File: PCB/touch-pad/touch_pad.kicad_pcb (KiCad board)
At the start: 2 copper layers, 60.6 x 50.7 mm, 13 parts

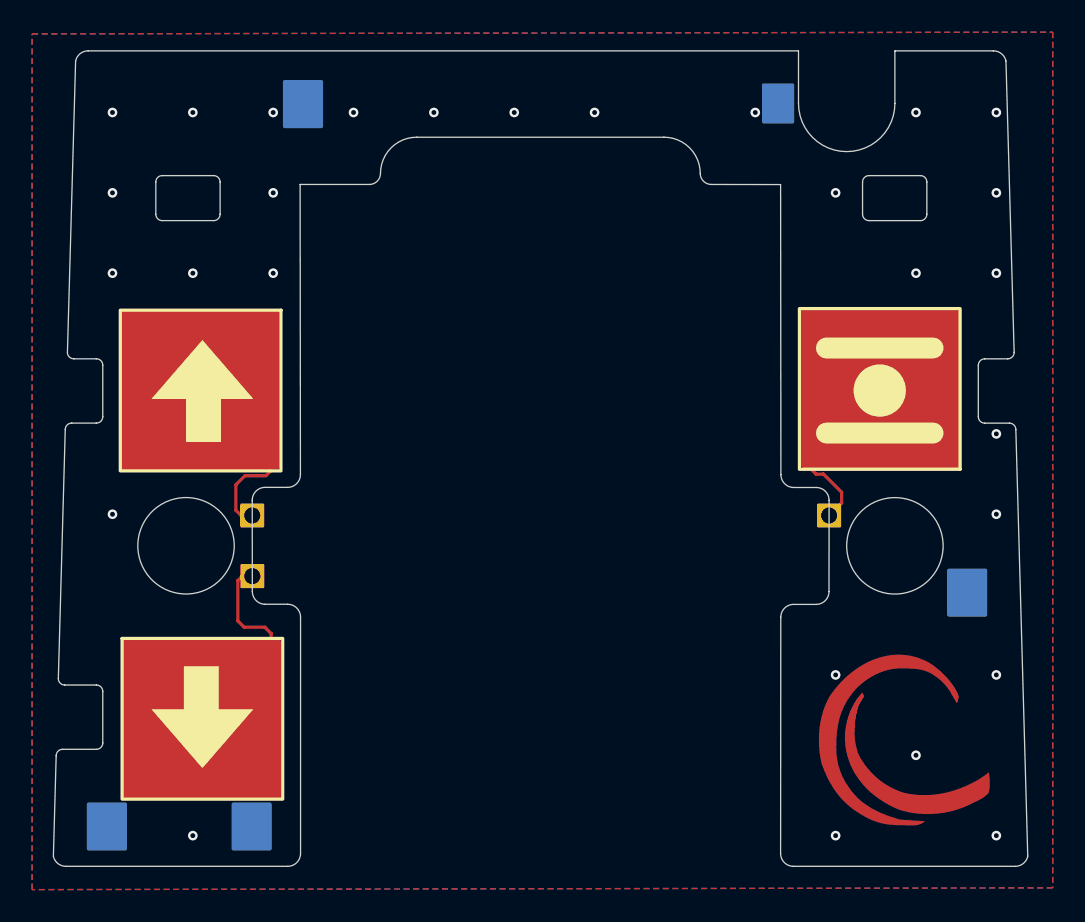
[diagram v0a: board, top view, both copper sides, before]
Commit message: Import v2.0 development state from Bitbucket branch v2.0
Overlay of the v2.0 design work onto the restructured PCB/ layout:
- airgradient-go-main v2.0 WIP: 186 footprints, microSD, PS1-CO,
  Birdy schematic review fixes; adds v2.0 BOM CSVs
- touch-pad v2.0: T1-T3 pads wired to touch controller CS channels,
  +3.1V rail renamed to VCC
- scd4x-module: minor updates
- libraries: new parts (SPL07-003, BM05B-SRSS-TB, PS1-CO, battery
  holder, ESP32-C5 models) and updated footprints; all library and
  3D model references normalized to ${KIPRJMOD}-relative paths
- led_pcb board was dropped in v2.0 (never migrated)

Known open items carried over from review: U14 VDD_IO not yet
connected to the 3.1V rail; U19 (LM66200) still fitted.
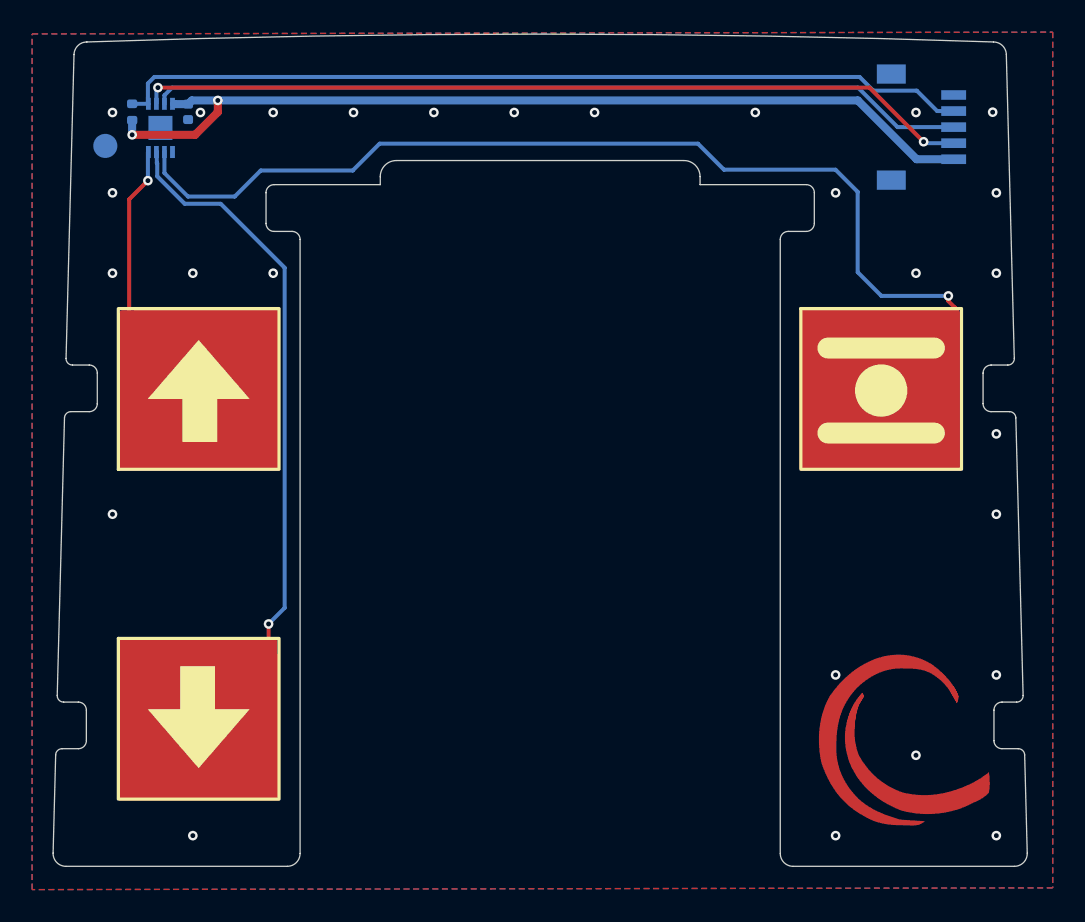
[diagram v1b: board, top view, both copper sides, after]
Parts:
- removed ? (x8): , 
- added C42: 0.1uF/25V, Capacitor_SMD:C_0402_1005Metric, B.Cu at (29.6, 25.2)
- added CN1: SM05B-SRSS-TB (LF)(SN), easyeda2kicad-oaf:CONN-SMD_SM05B-SRSS-TB-LF-SN, B.Cu at (75.3, 26.1)
- added R38: 100K, Resistor_SMD:R_0402_1005Metric, B.Cu at (26.1, 25.2)
- added TP1: TestPoint, TestPoint:TestPoint_Pad_D1.5mm, B.Cu at (24.4, 27.3)
- added U11: CAP1203-1-AC3-TR, easyeda2kicad-oaf:TDFN-8_L3.0-W2.0-P0.50-BL-EP, B.Cu at (27.9, 26.2)
- T1, T2, T3: footprint Library:tourch_pad -> Library-oaf:tourch_pad
- moved T1 0.34 mm to (30.1, 42.4), turned to 90 degrees
- moved T2 0.23 mm to (30.2, 62.8)
- moved T3 0.22 mm to (72.7, 42.3), turned to 0 degrees
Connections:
- T1 pad 1: unconnected-(T1-Pad1) -> Net-(U11-CS1)
- T2 pad 1: unconnected-(T2-Pad1) -> Net-(U11-CS2)
- T3 pad 1: unconnected-(T3-Pad1) -> Net-(U11-CS3)
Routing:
- net Net-(U11-CS3): track 0.00 -> 60.2 mm, vias 0 -> 1
- net VCC: track 0.00 -> 57.7 mm, vias 0 -> 2
- net /INT: track 0.00 -> 53.5 mm
- net /SDA: track 0.00 -> 52.0 mm, vias 0 -> 2
- net /SCL: track 0.00 -> 50.9 mm
- net Net-(U11-CS2): track 0.00 -> 36.0 mm, vias 0 -> 1
- net Net-(U11-CS1): track 0.00 -> 11.0 mm, vias 0 -> 1
- net unconnected-(T2-Pad1): track 6.96 -> 0.00 mm
- net unconnected-(T1-Pad1): track 5.98 -> 0.00 mm
- net unconnected-(T3-Pad1): track 4.94 -> 0.00 mm
- net GND: vias 28 -> 27
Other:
- board size 60.6 x 50.7 mm -> 60.6 x 51.8 mm
- board text added: "AG-TOUCH-GO-v2.0"
- board text removed: "${REFERENCE}"
- board text removed: "AG-TOUCH-GO-v1.0"

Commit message: Create production files; switch touch pad connector to Hong Cheng
Mainboard:
- Export v2.0 production files (gerbers, BOM, positions) and 3D STEP model
- Add BOM.csv export

Touch pad:
- Change CN1 connector manufacturer from JST to Hong Cheng HCZZ0032-5 (same housing)
- Regenerate production files as v2.0 (BOM now includes full parts list)
- Add Hong Cheng connector symbol, footprint, and 3D model to easyeda2kicad library
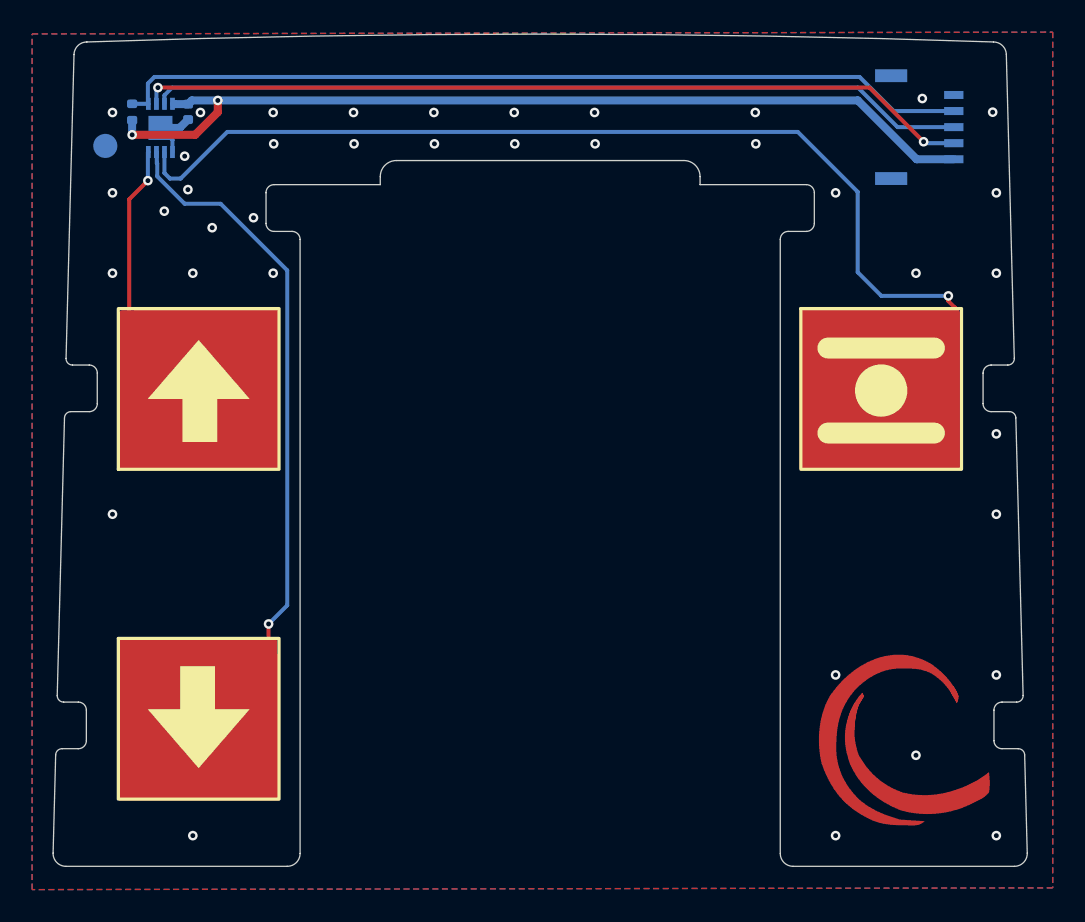
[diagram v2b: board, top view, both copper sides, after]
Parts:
- CN1: value SM05B-SRSS-TB (LF)(SN) -> HCZZ0032-5; footprint easyeda2kicad-oaf:CONN-SMD_SM05B-SRSS-TB-LF-SN -> easyeda2kicad-oaf:CONN-SMD_HCZZ0032-5
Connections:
- U11 pad 9: unconnected-(U11-EP-Pad9) -> GND
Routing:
- net GND: track 0.00 -> 3.75 mm, vias 27 -> 38

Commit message: touch-pad: add logo artwork
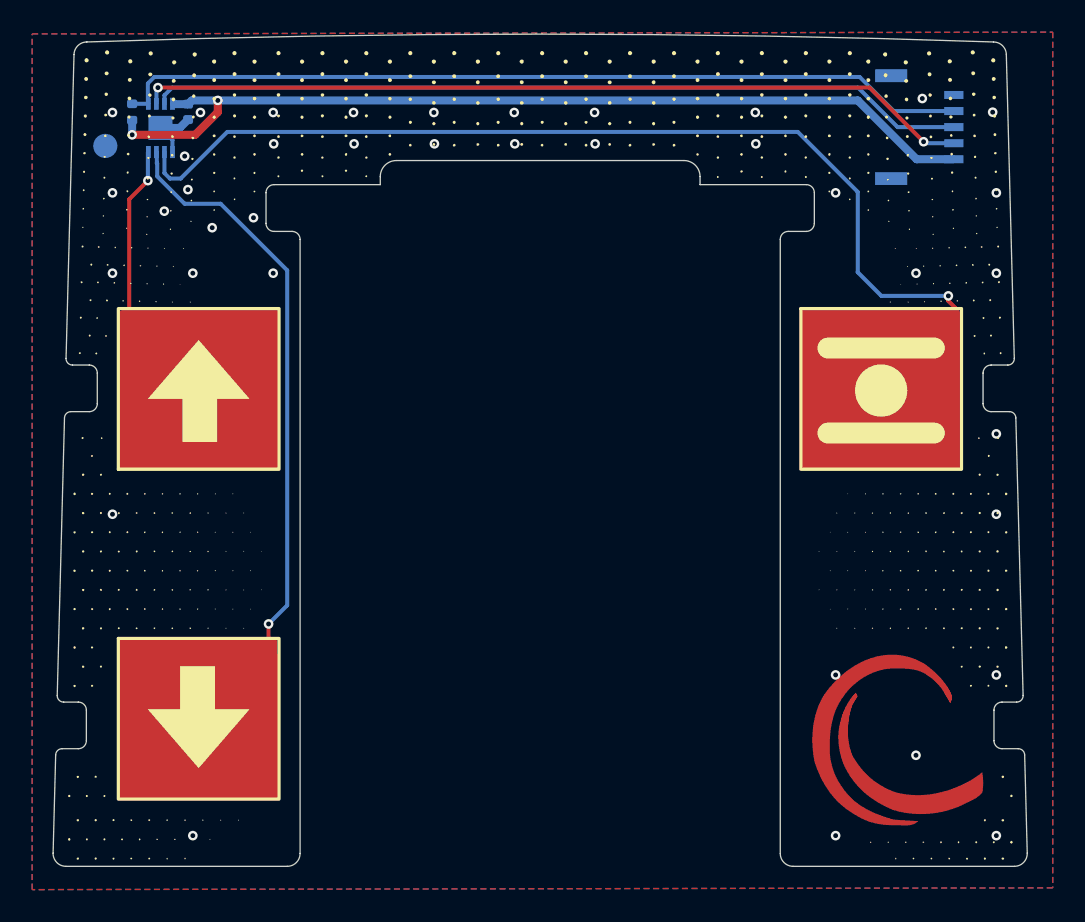
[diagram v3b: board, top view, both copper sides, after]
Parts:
- added G***: LOGO, LOGO, F.Cu at (51.4, 46.6)

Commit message: touch-pad v2.1: revision and silkscreen to v2.1, add v2.1 production files
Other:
- board text added: "AG-TOUCH-GO-v2.1"
- board text removed: "AG-TOUCH-GO-v2.0"
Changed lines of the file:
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@@
 		(title "Touch_sensor")
 		(date "2026-05-13")
-		(rev "v2.0")
+		(rev "v2.1")
 		(company "Airgradient")
 		(comment 1 "CC-BY-SA")
@@
 		(layer "Edge.Cuts")
 	)
-	(gr_text "AG-TOUCH-GO-v2.0"
+	(gr_text "AG-TOUCH-GO-v2.1"
 		(at 79.715464 70.847225 0)
 		(layer "B.SilkS")
